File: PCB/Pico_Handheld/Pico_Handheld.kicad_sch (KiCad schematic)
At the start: 15 parts, among them SW1 UP, SW2 SW_SPDT, SW3 DOWN, SW4 LEFT, SW5 RIGHT, SW6 B, SW7 A, U1 Pico, U2 Volume_Wheel, U3 0.91_128x64_SSD1306_Oled_Disp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

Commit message: V0.1.1 Finalised PCB V1.0
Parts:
- BZ1: footprint Buzzer_Beeper:Buzzer_12x9.5RM7.6 -> Buzzer_Beeper:MagneticBuzzer_ProSignal_ABT-410-RC
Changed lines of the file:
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@@
       (effects (font (size 1.27 1.27)) (justify left))
     )
-    (property "Footprint" "Buzzer_Beeper:Buzzer_12x9.5RM7.6" (id 2) (at 201.295 115.57 90)
+    (property "Footprint" "Buzzer_Beeper:MagneticBuzzer_ProSignal_ABT-410-RC" (id 2) (at 201.295 115.57 90)
       (effects (font (size 1.27 1.27)) hide)
     )
@@
     )
     (path "/5a2cef49-6d96-409b-81e9-d0c8373305c6"
-      (reference "BZ1") (unit 1) (value "Buzzer") (footprint "Buzzer_Beeper:Buzzer_12x9.5RM7.6")
+      (reference "BZ1") (unit 1) (value "Buzzer") (footprint "Buzzer_Beeper:MagneticBuzzer_ProSignal_ABT-410-RC")
     )
     (path "/cc69aa39-44c9-47d1-afe0-090d73e6a844"

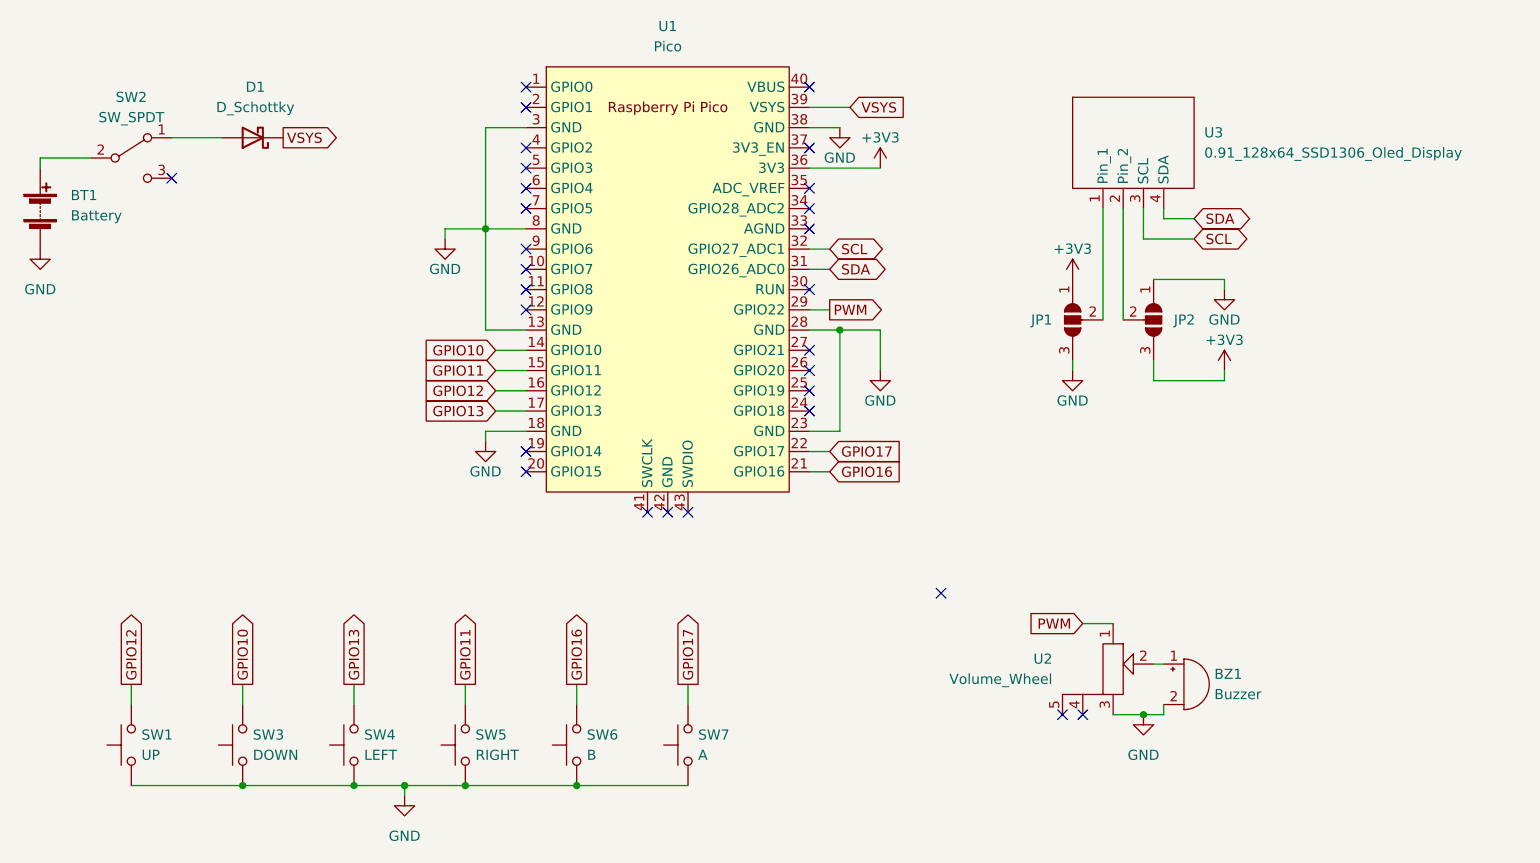
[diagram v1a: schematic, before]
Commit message: V0.2.0 Updated Schematic to Use an ILI9341 TFT LCD
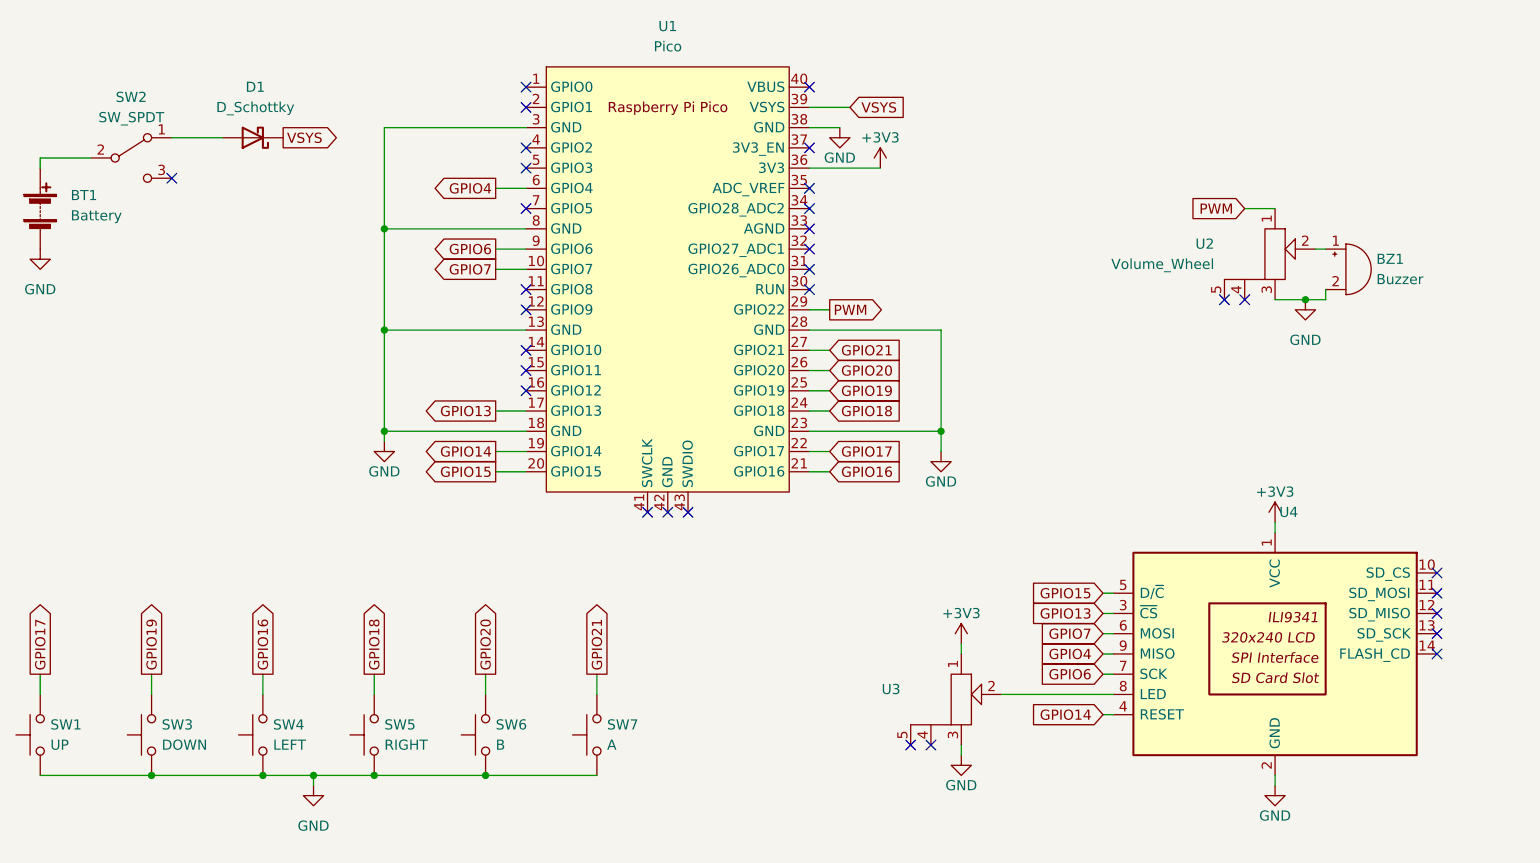
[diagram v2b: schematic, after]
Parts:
- removed JP1, JP2: SolderJumper_3_Open, Jumper:SolderJumper-3_P1.3mm_Open_Pad1.0x1.5mm, symbol Jumper:SolderJumper_3_Open
- removed U3: 0.91_128x64_SSD1306_Oled_Display, 0.91_128x64_SSD1306_Oled_Display:0.91_128x64_SSD1306_Oled_Display, symbol 0.91_128x64_SSD1306_Oled_Display:0.91_128x64_SSD1306_Oled_Display
- added U3: (no value), Volume_Wheel:Volume_Wheel, symbol Volume_Wheel:Volume_Wheel
- added U4: (no value), symbol Driver_Display:CR2013-MI2120
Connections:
- net +3V3: now also U3.1, U4.1 (VCC)
- net GND: now also U3.3, U4.2 (GND)
- net GPIO13: now also U4.3 (~{CS}); no longer SW4.2
- net GPIO16: now also SW4.2; no longer SW6.2
- net GPIO17: now also SW1.2; no longer SW7.2
- net GPIO7: now reaches U1.10 (GPIO7)
- net GPIO7: now also U4.6 (MOSI)
- net GPIO14: now reaches U1.19 (GPIO14)
- net GPIO14: now also U4.4 (RESET)
- net GPIO15: now reaches U1.20 (GPIO15)
- net GPIO15: now also U4.5 (D/~{C})
- net GPIO18: now reaches U1.24 (GPIO18)
- net GPIO18: now also SW5.2
- net GPIO19: now reaches U1.25 (GPIO19)
- net GPIO19: now also SW3.2
- net GPIO20: now reaches U1.26 (GPIO20)
- net GPIO20: now also SW6.2
- net GPIO21: now reaches U1.27 (GPIO21)
- net GPIO21: now also SW7.2
- net GPIO4: now reaches U1.6 (GPIO4)
- net GPIO4: now also U4.9 (MISO)
- net GPIO6: now reaches U1.9 (GPIO6)
- net GPIO6: now also U4.7 (SCK)
- net GPIO10: no longer names the net of U1.14 (GPIO10)
- net GPIO10: no longer SW3.2
- net GPIO11: no longer names the net of U1.15 (GPIO11)
- net GPIO11: no longer SW5.2
- net GPIO12: no longer names the net of U1.16 (GPIO12)
- net GPIO12: no longer SW1.2
- net SCL: no longer names the net of U1.32 (GPIO27_ADC1)
- net SDA: no longer names the net of U1.31 (GPIO26_ADC0)
- new net: U3.2, U4.8 (LED)
- no-connect marks 29 -> 31
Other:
- moved on the sheet: BZ1, SW1, SW3, SW4, SW5, SW6, SW7, U2
